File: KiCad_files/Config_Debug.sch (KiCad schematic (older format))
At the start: 54 parts, among them J3 Conn_01x06, J4 USB_C_Receptacle, SW1 SW_Push, U1 XC7A35T_CSG325, U10 W25Q128JV, U6 FT2232HL, U7 93LCxxC, U8 SiT8209, U9 SiT9102, Y1 12MHz

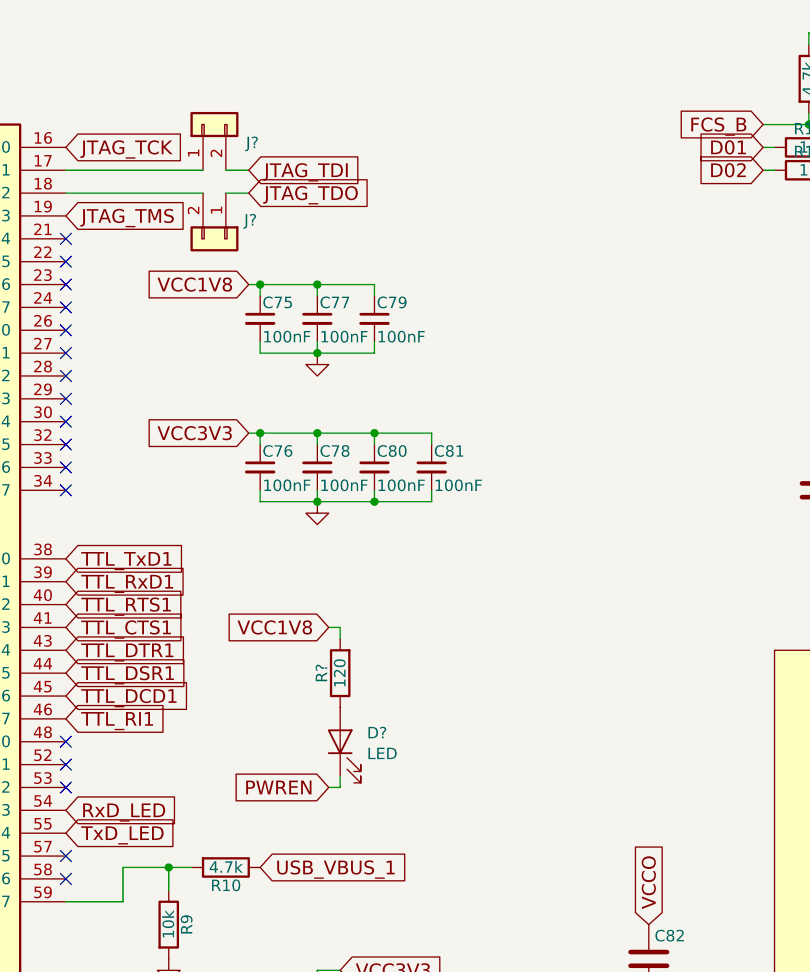
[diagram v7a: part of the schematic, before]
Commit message: Cleanup for DRC and HDMI. HDMI and DDR2 looks good
DRC returns 5 errors with POWEROUTPUT-POWEROUTPUT set as good.
3 of them come from 3V3 since it's being driven from a MOSFET.
1 of them from VCC5V0 not yet supplied.
1 of them from USB_VBUS not set as output.
TODO:
5V supply for HDMI
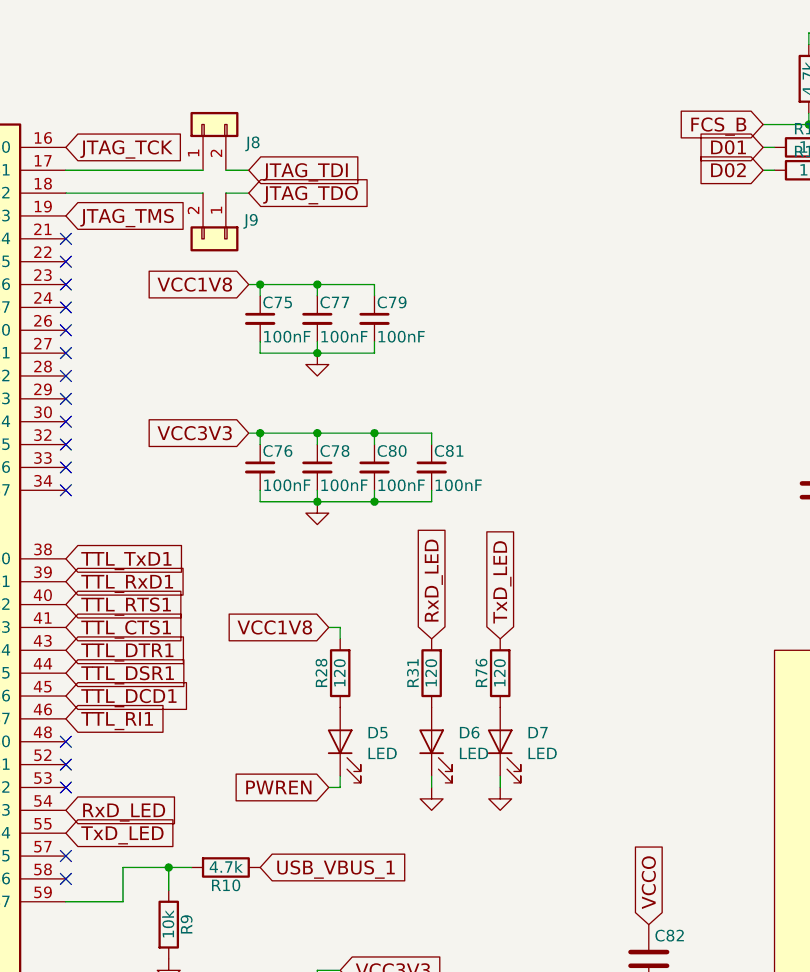
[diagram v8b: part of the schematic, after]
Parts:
- added D6, D7: LED, symbol Device:LED
- added R31, R76: 120, symbol Device:R
- gave numbers to parts that had none: 4
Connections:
- net GND: now also D6.1 (K), D7.1 (K)
- net RxD_LED: now also R31.2
- net TxD_LED: now also R76.2
- new net: D7.2 (A), R76.1
- new net: D6.2 (A), R31.1
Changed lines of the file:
@@
 U 1 1 5C174B0F
 P 8300 5600
+AR Path="/5C174B0F" Ref="U1"  Part="1"
+AR Path="/5C0630AC/5C174B0F" Ref="U1"  Part="1"
 F 0 "U1" H 8300 5300 60  0000 C CNN
 F 1 "XC7A35T_CSG325" H 8300 5400 60  0000 C CNN
@@
 U 1 1 5C176AC1
 P 8900 2900
+AR Path="/5C176AC1" Ref="U9"  Part="1"
+AR Path="/5C0630AC/5C176AC1" Ref="U9"  Part="1"
 F 0 "U9" H 8900 3150 60  0000 C CNN
 F 1 "SiT9102" H 8900 2650 60  0000 C CNN
@@
 Wire Wire Line
 	900  6650 1200 6650
-Wire Wire Line
-	1800 5050 2000 5050
 NoConn ~ 4850 1700
 NoConn ~ 4850 1800
@@
 	6800 5400 6800 5500
 $Comp
-L Device:LED D?
+L Device:LED D5
 U 1 1 5C7C445B
 P 6050 3900
-F 0 "D?" V 6088 3783 50  0000 R CNN
+F 0 "D5" V 6088 3783 50  0000 R CNN
 F 1 "LED" V 5997 3783 50  0000 R CNN
 F 2 "" H 6050 3900 50  0001 C CNN
@@
 $EndComp
 $Comp
-L Device:R R?
+L Device:R R28
 U 1 1 5C7C45F5
 P 6050 3600
-F 0 "R?" V 6130 3600 50  0000 C CNN
+F 0 "R28" V 6130 3600 50  0000 C CNN
 F 1 "120" V 6050 3600 50  0000 C CNN
 F 2 "" V 5980 3600 50  0001 C CNN
@@
 NoConn ~ 4850 5100
 $Comp
-L Connector_Generic:Conn_01x02 J?
+L Connector_Generic:Conn_01x02 J9
 U 1 1 5C82FBE2
 P 5550 1700
-F 0 "J?" V 5469 1780 50  0000 L CNN
+F 0 "J9" V 5469 1780 50  0000 L CNN
 F 1 "Conn_01x02" H 5630 1601 50  0001 L CNN
 F 2 "" H 5550 1700 50  0001 C CNN
@@
 $EndComp
 $Comp
-L Connector_Generic:Conn_01x02 J?
+L Connector_Generic:Conn_01x02 J8
 U 1 1 5C82FC7A
 P 5450 1200
-F 0 "J?" V 5370 1012 50  0000 R CNN
+F 0 "J8" V 5370 1012 50  0000 R CNN
 F 1 "Conn_01x02" H 5530 1101 50  0001 L CNN
 F 2 "" H 5450 1200 50  0001 C CNN
@@
 Wire Wire Line
 	5450 1500 4850 1500
+$Comp
+L Device:LED D7
+U 1 1 5C8DAB23
+P 6750 3900
+F 0 "D7" V 6788 3783 50  0000 R CNN
+F 1 "LED" V 6697 3783 50  0000 R CNN
+F 2 "" H 6750 3900 50  0001 C CNN
+F 3 "~" H 6750 3900 50  0001 C CNN
+	1    6750 3900
+	0    -1   -1   0
+$EndComp
+$Comp
+L Device:R R76
+U 1 1 5C8DAB29
+P 6750 3600
+F 0 "R76" V 6830 3600 50  0000 C CNN
+F 1 "120" V 6750 3600 50  0000 C CNN
+F 2 "" V 6680 3600 50  0001 C CNN
+F 3 "" H 6750 3600 50  0001 C CNN
+	1    6750 3600
+	-1   0    0    1
+$EndComp
+Wire Wire Line
+	6750 4100 6750 4050
+$Comp
+L power:GND #PWR0108
+U 1 1 5C8EC84C
+P 6750 4100
+F 0 "#PWR0108" H 6750 3850 50  0001 C CNN
+F 1 "GND" H 6750 3950 50  0001 C CNN
+F 2 "" H 6750 4100 50  0001 C CNN
+F 3 "" H 6750 4100 50  0001 C CNN
+	1    6750 4100
+	1    0    0    -1
+$EndComp
+Text GLabel 6750 3450 1    60   Input ~ 0
+TxD_LED
+$Comp
+L Device:LED D6
+U 1 1 5C8ECAE1
+P 6450 3900
+F 0 "D6" V 6488 3783 50  0000 R CNN
+F 1 "LED" V 6397 3783 50  0000 R CNN
+F 2 "" H 6450 3900 50  0001 C CNN
+F 3 "~" H 6450 3900 50  0001 C CNN
+	1    6450 3900
+	0    -1   -1   0
+$EndComp
+$Comp
+L Device:R R31
+U 1 1 5C8ECAE7
+P 6450 3600
+F 0 "R31" V 6530 3600 50  0000 C CNN
+F 1 "120" V 6450 3600 50  0000 C CNN
+F 2 "" V 6380 3600 50  0001 C CNN
+F 3 "" H 6450 3600 50  0001 C CNN
+	1    6450 3600
+	-1   0    0    1
+$EndComp
+Wire Wire Line
+	6450 4100 6450 4050
+$Comp
+L power:GND #PWR0109
+U 1 1 5C8ECAEE
+P 6450 4100
+F 0 "#PWR0109" H 6450 3850 50  0001 C CNN
+F 1 "GND" H 6450 3950 50  0001 C CNN
+F 2 "" H 6450 4100 50  0001 C CNN
+F 3 "" H 6450 4100 50  0001 C CNN
+	1    6450 4100
+	1    0    0    -1
+$EndComp
+Text GLabel 6450 3450 1    60   Input ~ 0
+RxD_LED
+Wire Wire Line
+	1800 5050 2000 5050
 $EndSCHEMATC
